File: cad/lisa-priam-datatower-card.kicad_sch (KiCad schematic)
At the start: 67 parts, among them J1 Lisa Expansion Card Edge, P2 DB25_Receptacle_MountingHoles

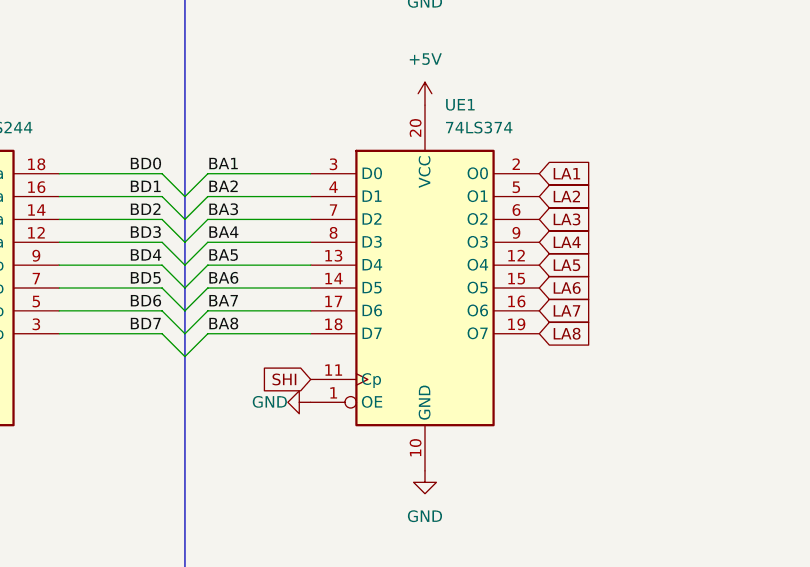
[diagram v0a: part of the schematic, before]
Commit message: Correction: LA6 changed to LAA on LS374
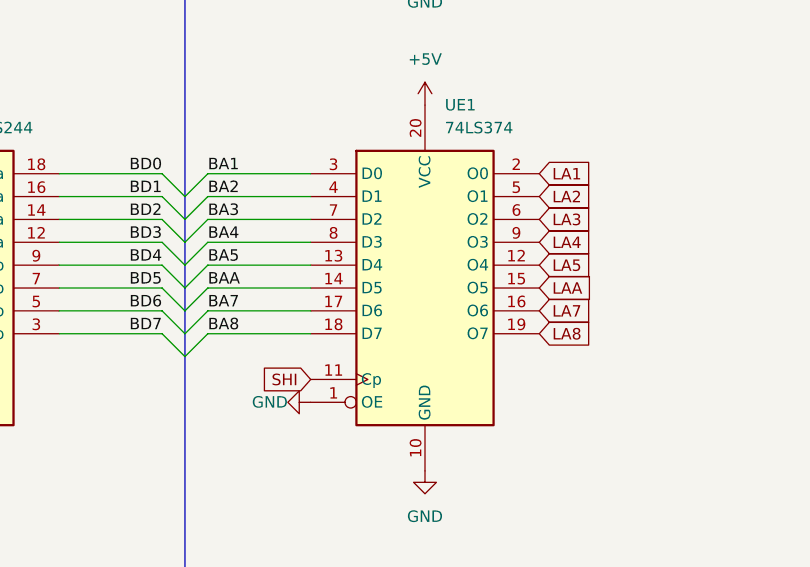
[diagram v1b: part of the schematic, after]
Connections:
- net LA6 is gone; now on net LAA: UE1.15 (O5)
- net BA6: no longer UE1.14 (D5)
- net BAA: now also UE1.14 (D5)
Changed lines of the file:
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@@
     (effects (font (size 1.27 1.27)) (justify left bottom))
   )
-  (label "BA6" (at 466.09 187.96 0) (fields_autoplaced)
+  (label "BAA" (at 466.09 187.96 0) (fields_autoplaced)
     (effects (font (size 1.27 1.27)) (justify left bottom))
   )
@@
     )
   )
-  (global_label "LA6" (shape input) (at 502.92 187.96 0) (fields_autoplaced)
-    (effects (font (size 1.27 1.27)) (justify left))
-    (property "Intersheetrefs" "${INTERSHEET_REFS}" (at 509.2314 187.96 0)
-      (effects (font (size 1.27 1.27)) (justify left) hide)
-    )
+  (global_label "LAA" (shape input) (at 502.92 187.96 0) (fields_autoplaced)
+    (effects (font (size 1.27 1.27)) (justify left))
+    (property "Intersheetrefs" "${INTERSHEET_REFS}" (at 509.1105 187.96 0)
+      (effects (font (size 1.27 1.27)) (justify left) hide)
+    )
